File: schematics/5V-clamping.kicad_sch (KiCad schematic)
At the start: 4 parts

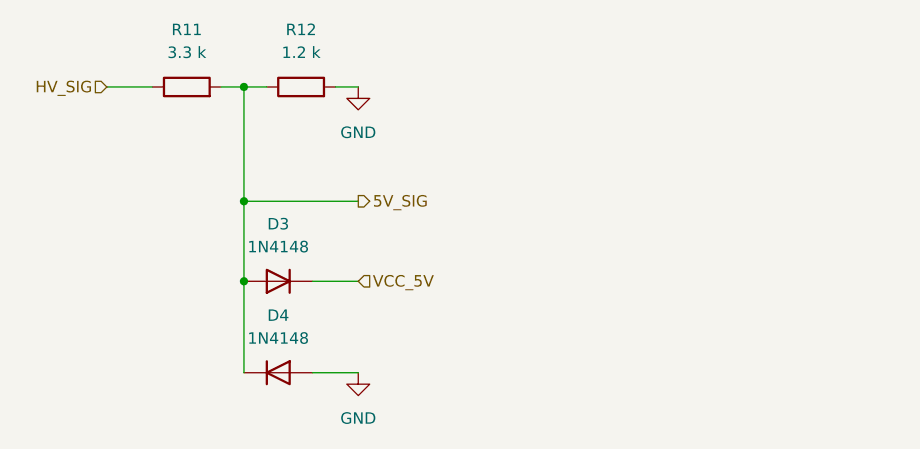
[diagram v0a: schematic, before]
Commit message: OBD II clamping schematic simplification; README file update. Small repositionings.
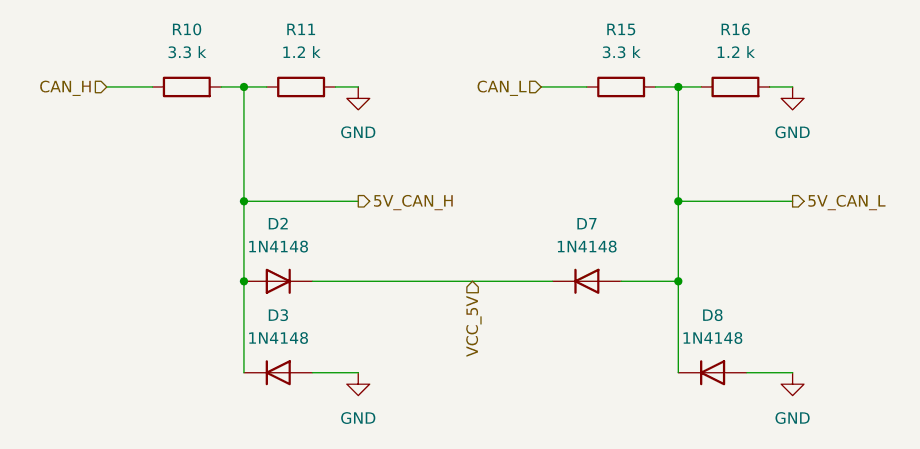
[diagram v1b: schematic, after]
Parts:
- added D7, D8: 1N4148, Diode_THT:D_DO-35_SOD27_P7.62mm_Horizontal, symbol Diode:1N4148
- added R15: 3.3 k, symbol Device:R
- added R16: 1.2 k, symbol Device:R
- renumbered D3 to D2, D4 to D3, R11 to R10, R12 to R11
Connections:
- net GND: now also D8.2 (A), R16.2
- net VCC_5V: now also D7.1 (K)
- net 5V_SIG renamed 5V_CAN_H
- net HV_SIG renamed CAN_H
- new net 5V_CAN_L: D7.2 (A), D8.1 (K), R15.2, R16.1
- new net CAN_L: R15.1
